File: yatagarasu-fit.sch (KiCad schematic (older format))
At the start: 47 parts, among them P1 96B_LS_CONN_02X20, P2 +12V_IN, P3 ttyAMA2, Q1 MMBT3904, Q2 MMBT3904, SW1 RESET, U1 8T245, U2 8T245, U3 PCA9306, U4 PCA9306

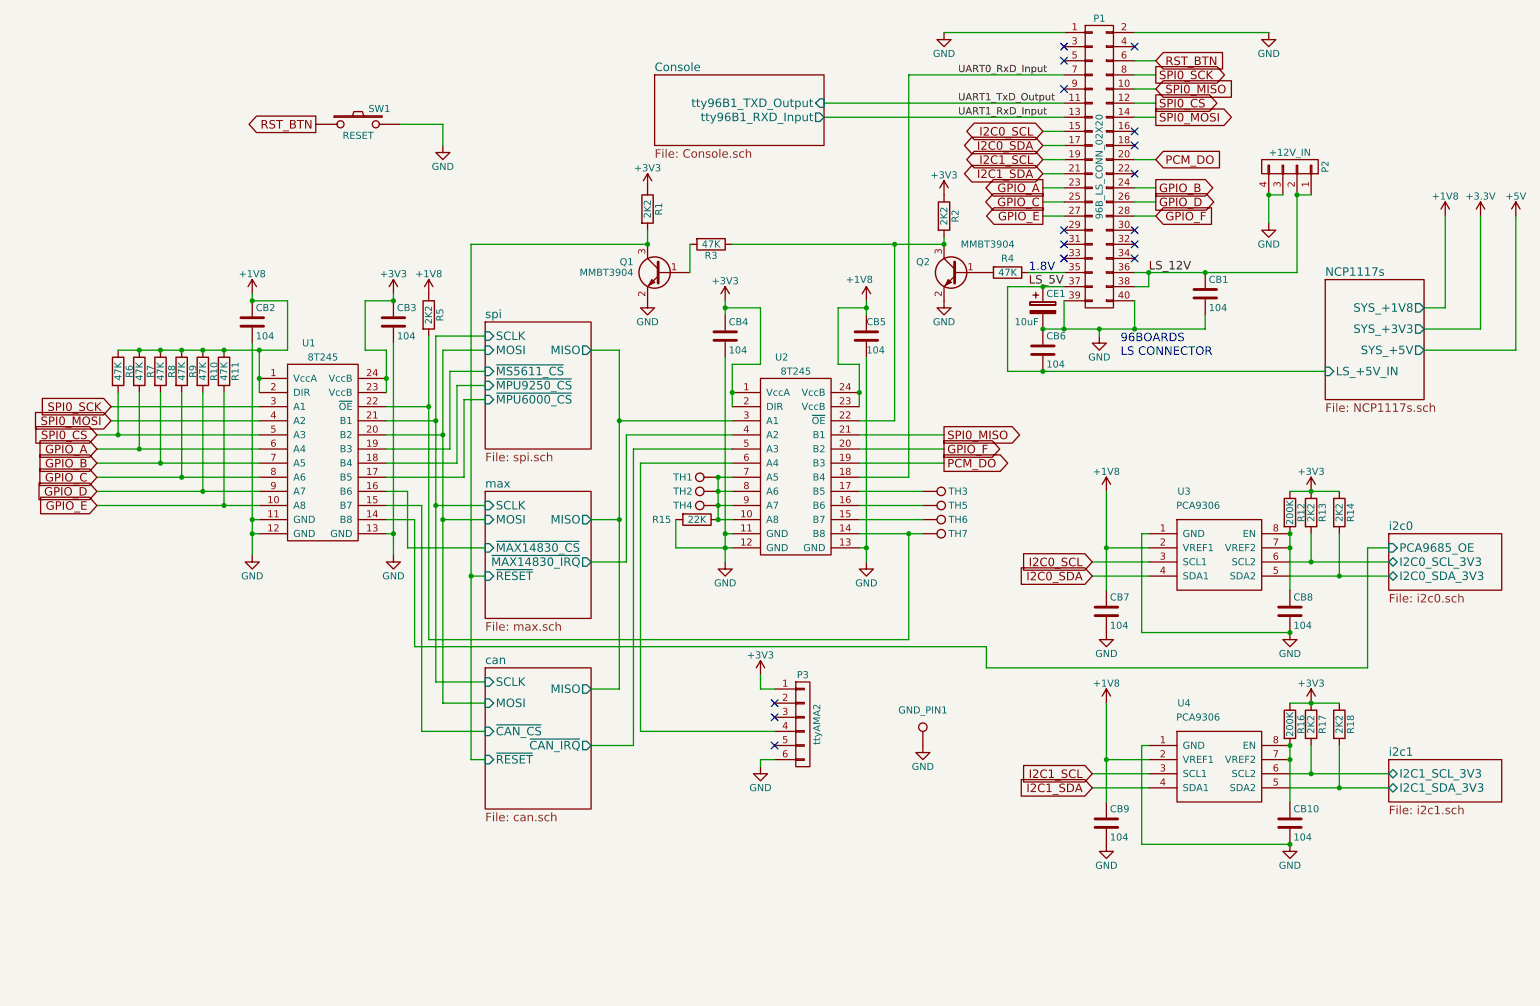
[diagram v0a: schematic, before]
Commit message: Updated schematic to improve compatibility with DB410C
Signed-off-by: Akira Tsukamoto <akira-t@s9.dion.ne.jp>
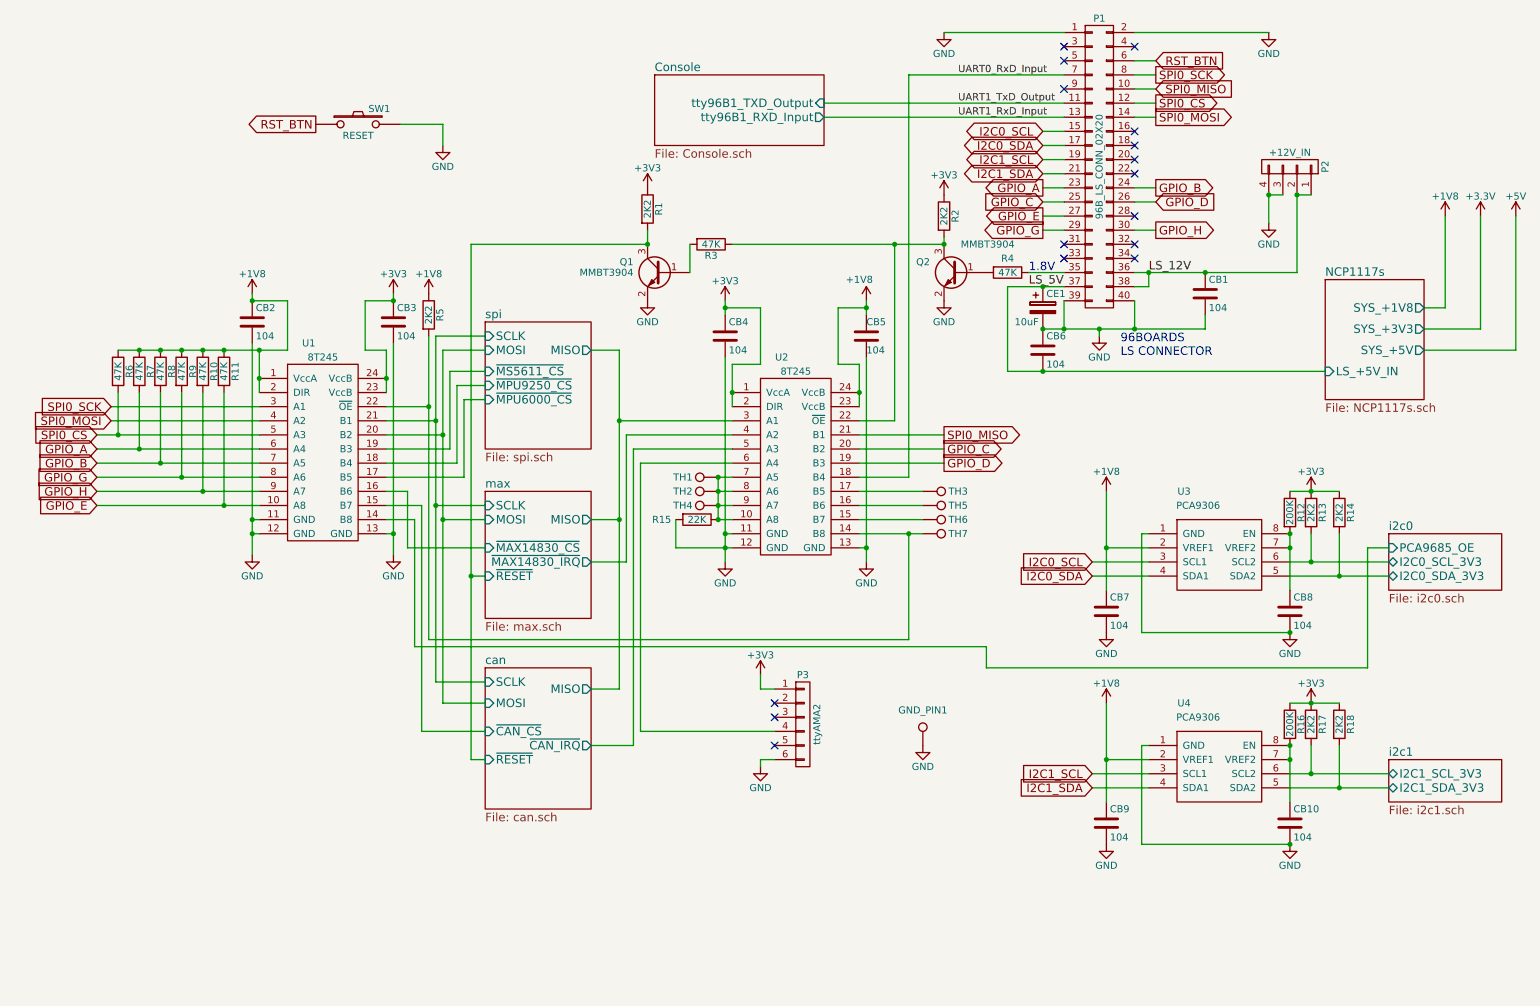
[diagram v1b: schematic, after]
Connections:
- net GPIO_C: now also U2.20 (B2); no longer R9.2, U1.8 (A6)
- net GPIO_D: now also U2.19 (B3); no longer R10.2, U1.9 (A7)
- net GPIO_G: now reaches P1.29 (P29)
- net GPIO_G: now also R9.2, U1.8 (A6)
- net GPIO_H: now reaches P1.30 (P30)
- net GPIO_H: now also R10.2, U1.9 (A7)
- net GPIO_F: no longer names the net of P1.28 (P28)
- net GPIO_F: no longer U2.20 (B2)
- net PCM_DO: no longer names the net of P1.20 (P20)
- net PCM_DO: no longer U2.19 (B3)
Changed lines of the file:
@@
 Text GLabel 8450 1300 2    60   Output ~ 0
 SPI0_MOSI
-Text GLabel 8450 2000 2    60   Input ~ 0
-GPIO_F
 Text GLabel 7650 2000 0    60   Output ~ 0
 GPIO_E
@@
 GPIO_B
 Text GLabel 950  3850 0    60   Input ~ 0
-GPIO_C
+GPIO_G
 Text GLabel 950  3950 0    60   Input ~ 0
-GPIO_D
+GPIO_H
 Text GLabel 950  4050 0    60   Input ~ 0
 GPIO_E
 Text GLabel 6950 3650 2    60   Output ~ 0
-GPIO_F
+GPIO_C
 Text GLabel 6950 3550 2    60   Output ~ 0
 SPI0_MISO
@@
 Text GLabel 950  3550 0    60   Input ~ 0
 SPI0_CS
-Text GLabel 7650 1900 0    60   Output ~ 0
+Text GLabel 7650 1900 0    60   Input ~ 0
 GPIO_C
-Text GLabel 8450 1900 2    60   Output ~ 0
+Text GLabel 8450 1900 2    60   Input ~ 0
 GPIO_D
 $Comp
@@
 $EndComp
 Text GLabel 6950 3750 2    60   Output ~ 0
-PCM_DO
+GPIO_D
 $Comp
 L R R4
@@
 NoConn ~ 7800 900
 NoConn ~ 7800 1100
-NoConn ~ 7800 2100
 NoConn ~ 7800 2200
 NoConn ~ 7800 2300
 NoConn ~ 8300 2300
 NoConn ~ 8300 2200
-NoConn ~ 8300 2100
 NoConn ~ 5750 5450
 NoConn ~ 5750 5750
@@
 	1    0    0    -1
 $EndComp
-Text GLabel 8450 1600 2    60   Input ~ 0
-PCM_DO
 NoConn ~ 8300 1700
 NoConn ~ 8300 1500
@@
 	8300 1300 8450 1300
 Wire Wire Line
-	8300 2000 8450 2000
-Wire Wire Line
 	7650 2000 7800 2000
 Wire Wire Line
@@
 Connection ~ 9250 1850
 Connection ~ 6950 2200
-Wire Wire Line
-	8300 1600 8450 1600
 Wire Wire Line
 	10350 2950 11000 2950
@@
 Text Label 7050 1300 0    51   ~ 0
 UART1_RxD_Input
+Text GLabel 7650 2100 0    60   Output ~ 0
+GPIO_G
+Wire Wire Line
+	7800 2100 7650 2100
+Text GLabel 8450 2100 2    60   Output ~ 0
+GPIO_H
+Wire Wire Line
+	8300 2100 8450 2100
+NoConn ~ 8300 1600
+NoConn ~ 8300 2000
 $EndSCHEMATC

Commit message: Improved the pin comatibility to match with other ardupilot project.
Signed-off-by: Akira Tsukamoto <akira-t@s9.dion.ne.jp>
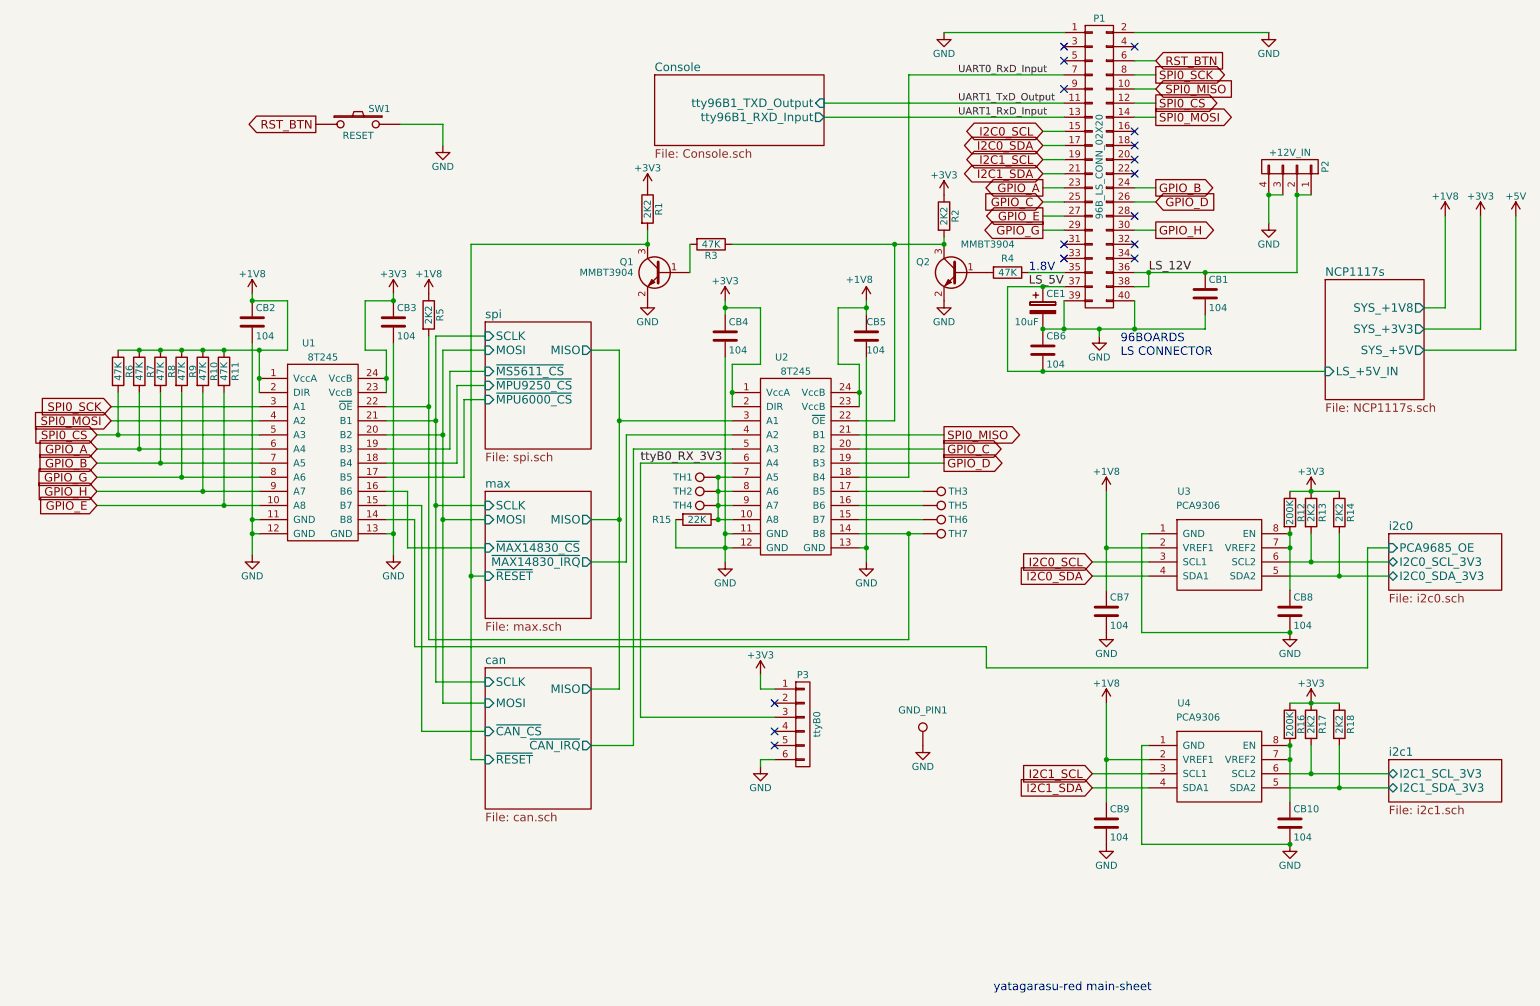
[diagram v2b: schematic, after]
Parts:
- P3: value ttyAMA2 -> ttyB0
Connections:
- net ttyB0_RX_3V3: now reaches P3.3 (P3)
- net ttyB0_RX_3V3: now also U2.6 (A4)
- net at P3.4 (P4): no longer U2.6 (A4)
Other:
- note added: "yatagarasu-red main-sheet"
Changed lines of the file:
@@
 P 5950 5600
 F 0 "P3" H 5950 5950 50  0000 C CNN
-F 1 "ttyAMA2" V 6050 5600 50  0000 C CNN
+F 1 "ttyB0" V 6050 5600 50  0000 C CNN
 F 2 "droneworks:GH_6P_side_droneworks" H 5950 5600 60  0001 C CNN
 F 3 "" H 5950 5600 60  0000 C CNN
@@
 	1    0    0    -1
 $EndComp
-NoConn ~ 5750 5550
 $Comp
 L TEST_1P GND_PIN1
@@
 $EndComp
 $Comp
-L +3.3V #PWR031
-U 1 1 57E09207
-P 10750 2000
-F 0 "#PWR031" H 10750 1850 50  0001 C CNN
-F 1 "+3.3V" H 10750 2140 50  0000 C CNN
-F 2 "" H 10750 2000 50  0000 C CNN
-F 3 "" H 10750 2000 50  0000 C CNN
-	1    10750 2000
-	1    0    0    -1
-$EndComp
-$Comp
-L +1V8 #PWR032
+L +1V8 #PWR031
 U 1 1 57E09321
 P 10500 2000
-F 0 "#PWR032" H 10500 1850 50  0001 C CNN
+F 0 "#PWR031" H 10500 1850 50  0001 C CNN
 F 1 "+1V8" H 10500 2140 50  0000 C CNN
 F 2 "" H 10500 2000 50  0000 C CNN
@@
 	4800 3750 5450 3750
 Wire Wire Line
-	4800 3750 4800 5650
+	4800 3750 4800 5550
 Wire Wire Line
 	4750 3650 5450 3650
@@
 	4700 3550 5450 3550
 Wire Wire Line
-	4800 5650 5750 5650
-Wire Wire Line
 	8300 2800 8300 2600
 Connection ~ 8800 2400
@@
 	5350 4150 5450 4150
 Wire Wire Line
-	5450 4050 5350 4050
+	5350 4050 5450 4050
 Wire Wire Line
 	5350 3950 5450 3950
@@
 	7800 2600 7800 2800
 Wire Wire Line
-	9650 3100 7400 3100
+	7400 3100 9650 3100
 Wire Wire Line
 	7400 2500 7800 2500
@@
 NoConn ~ 8300 1600
 NoConn ~ 8300 2000
+Text Notes 7300 7500 0    60   ~ 0
+yatagarasu-red main-sheet
+Text Label 4800 3750 0    60   ~ 0
+ttyB0_RX_3V3
+Wire Wire Line
+	4800 5550 5750 5550
+NoConn ~ 5750 5650
+$Comp
+L +3V3 #PWR032
+U 1 1 5A332190
+P 10750 2000
+F 0 "#PWR032" H 10750 1850 50  0001 C CNN
+F 1 "+3V3" H 10750 2140 50  0000 C CNN
+F 2 "" H 10750 2000 50  0000 C CNN
+F 3 "" H 10750 2000 50  0000 C CNN
+	1    10750 2000
+	1    0    0    -1
+$EndComp
 $EndSCHEMATC
